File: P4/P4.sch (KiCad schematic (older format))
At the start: 113 parts, among them J1 Conn_01x10, J11 Conn_01x10, J12 Conn_01x10, J13 Conn_01x25, J14 Conn_01x25, J15 Conn_01x25, J16 Conn_01x25, J17 Conn_01x25, J18 Conn_01x25, J19 Conn_01x25, J2 Conn_01x10, J20 Conn_01x25, J26 Conn_01x01, J3 Conn_01x10, J4 Conn_01x10, J5 Conn_01x05, J6 Conn_01x10, J7 Conn_01x10, J8 Conn_01x03, J9 Conn_01x03, Q1 BC212L, Q2 BC212L, Q3 TIP42, Q4 TIP41, U1 LM723_DIP14, U10 LM13600, U11 LF353, U12 LM741, U13 LM13600, U2 LM741, U3 L7905, U4 LM1458, U5 LM1458, U6 LF353, U7 LM13600, U8 LF353, U9 LF353

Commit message: PS4 pcb layout
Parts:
- added H1, H10, H2, H3, H4, H5, H6, H7, H8, H9: MountingHole, MountingHole:MountingHole_3.2mm_M3_Pad, symbol Mechanical:MountingHole
- added HS1, HS2, HS3: Heatsink, Heatsink:Heatsink_Stonecold_HS-132_32x14mm_2xFixation1.5mm, symbol Mechanical:Heatsink
- C1, C13, C14, C2, C3, C4, C8, CA15, CA17, CA19, CA21, CB16, CB18, CB20, CB22: footprint (none) -> Capacitor_THT:C_Disc_D5.0mm_W2.5mm_P5.00mm
- C10, C11, C12, C7, C9: footprint (none) -> Capacitor_THT:CP_Radial_D6.3mm_P2.50mm
- C5, C6: footprint (none) -> Capacitor_THT:CP_Axial_L20.0mm_D13.0mm_P26.00mm_Horizontal
- D5, D6: footprint (none) -> Diode_THT:D_DO-15_P12.70mm_Horizontal
- J1, J11, J12, J2, J3, J4: footprint (none) -> Connector_PinHeader_2.54mm:PinHeader_1x10_P2.54mm_Vertical
- J13, J14, J15, J16, J17, J18, J19, J20: footprint (none) -> Connector_PinSocket_2.54mm:PinSocket_1x25_P2.54mm_Vertical
- J26: footprint (none) -> Connector_Wire:SolderWire-1.5sqmm_1x01_D1.7mm_OD3.9mm
- J5: footprint (none) -> Connector_PinHeader_2.54mm:PinHeader_1x05_P2.54mm_Vertical
- J6: renamed from J7; footprint (none) -> Connector_PinHeader_2.54mm:PinHeader_1x10_P2.54mm_Vertical
- J7: renamed from J6; footprint (none) -> Connector_PinHeader_2.54mm:PinHeader_1x10_P2.54mm_Vertical
- J8, J9: footprint (none) -> Connector_PinHeader_2.54mm:PinHeader_1x03_P2.54mm_Vertical
- Q1, Q2: footprint (none) -> Package_TO_SOT_THT:TO-92L_Wide
- R1, R10, R11, R12, R13, R14, R15, R16, R17, R18, R19, R2, R20, R21, R22, R23, R24, R25, R26, R27, R28, R29, R3, R4, R42, R43, R44, R5, R6, R7, R8, R9, RA30, RA33, RA36, RA39, RB31, RB34, RB37, RB40, RC32, RC35, RC38, RC41: footprint (none) -> Resistor_THT:R_Axial_DIN0207_L6.3mm_D2.5mm_P7.62mm_Horizontal
- RV1: footprint (none) -> Potentiometer_THT:Potentiometer_Bourns_3296Y_Vertical
- U10, U13, U7: footprint (none) -> Package_DIP:DIP-16_W7.62mm_Socket_LongPads
- U11, U12, U2, U4, U5, U6, U8, U9: footprint (none) -> Package_DIP:DIP-8_W7.62mm_Socket_LongPads
- U3: footprint (none) -> Package_TO_SOT_THT:TO-220-3_Vertical
- ZD1, ZD2: footprint (none) -> Diode_THT:D_DO-15_P10.16mm_Horizontal
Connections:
- net GNDA is gone; now on net GND: J6.10 (Pin_10), J6.9 (Pin_9), J7.5 (Pin_5), J7.6 (Pin_6)
- net at RV1.1: now also R14.1; no longer R13.2
- net at RV1.3: now also R13.2; no longer R14.1
- net 12_VCA_D renamed 14_VCA_D
- net 14_VCA_D: now also J2.4 (Pin_4); no longer J2.2 (Pin_2)
- net 14_VCA_R renamed 12_VCA_R
- net 12_VCA_R: now also J2.2 (Pin_2); no longer J2.4 (Pin_4)
- net U1_PIN10: no longer names the net of Q4.1 (B), U1.10 (Vout)
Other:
- moved on the sheet: J6, J7

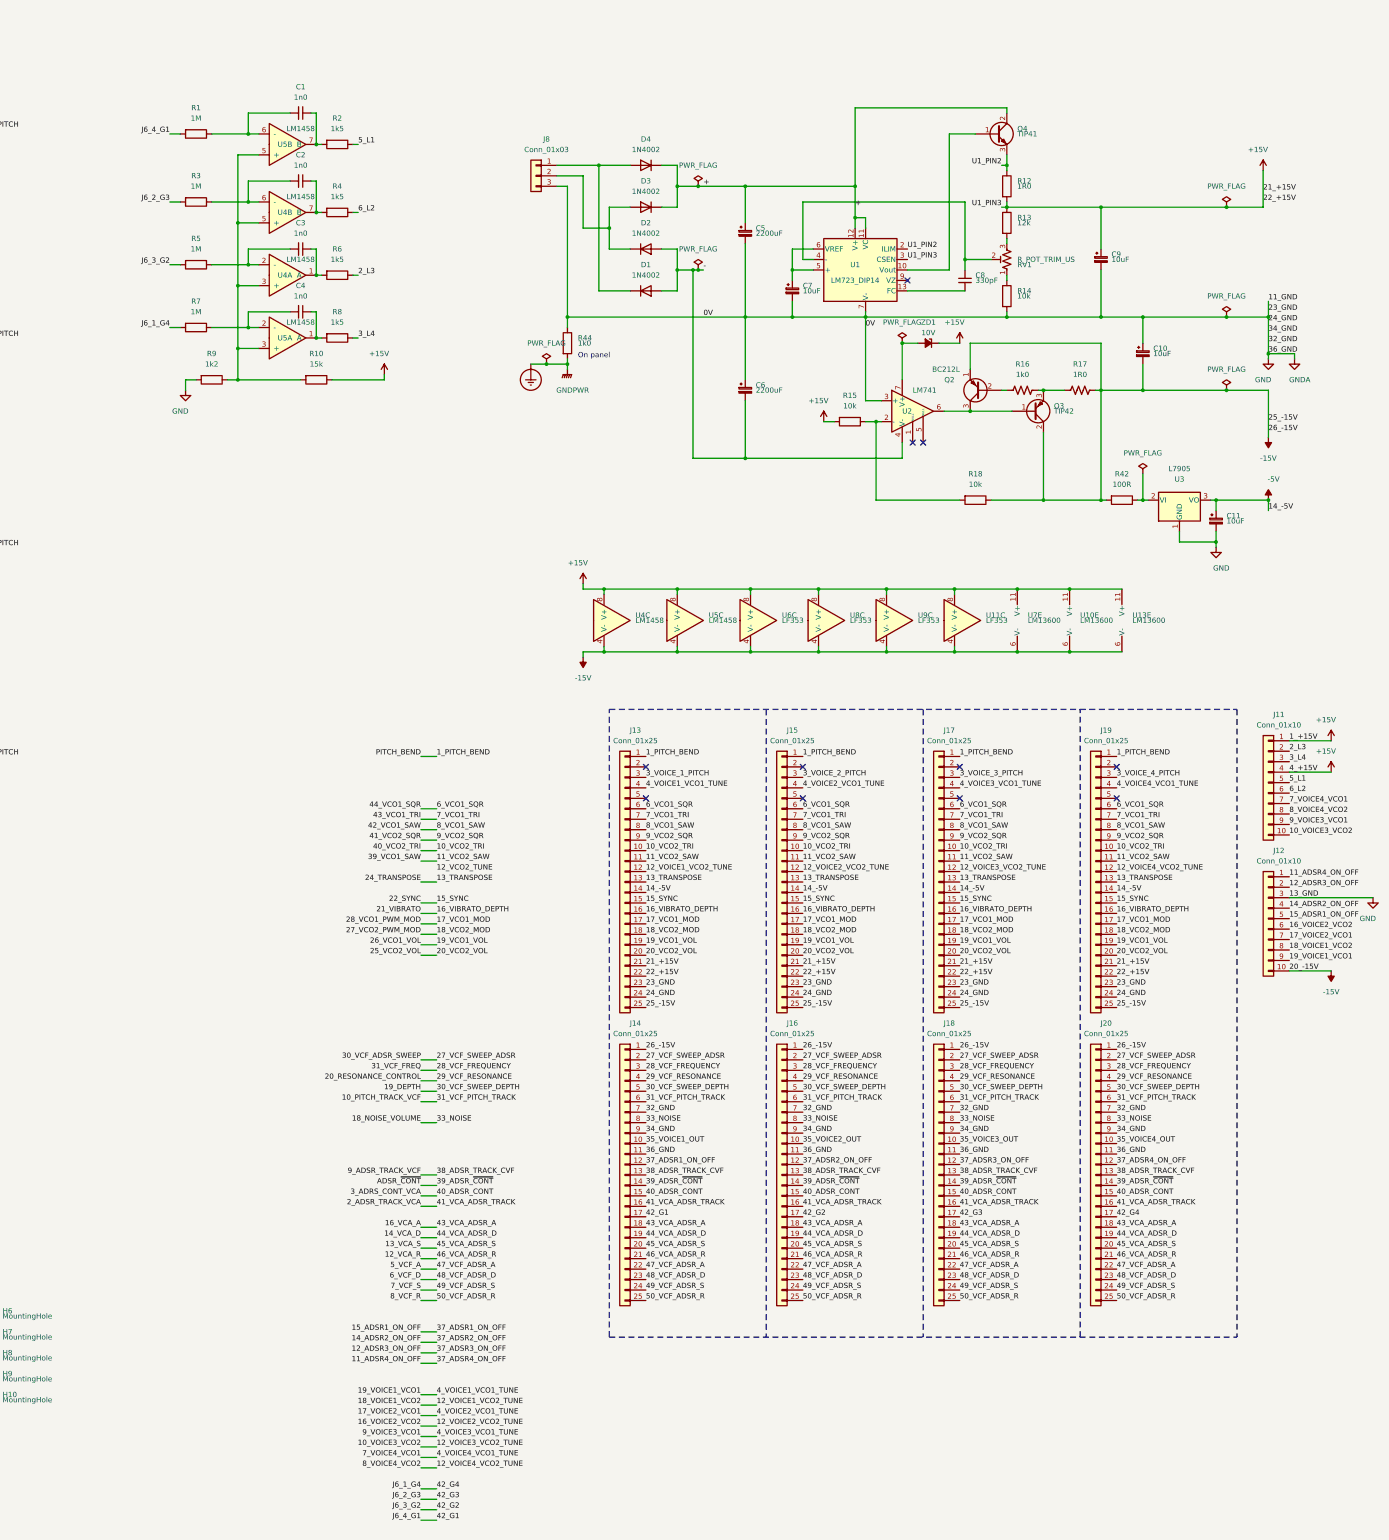
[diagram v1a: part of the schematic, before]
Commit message: Update PS4 board/schematic
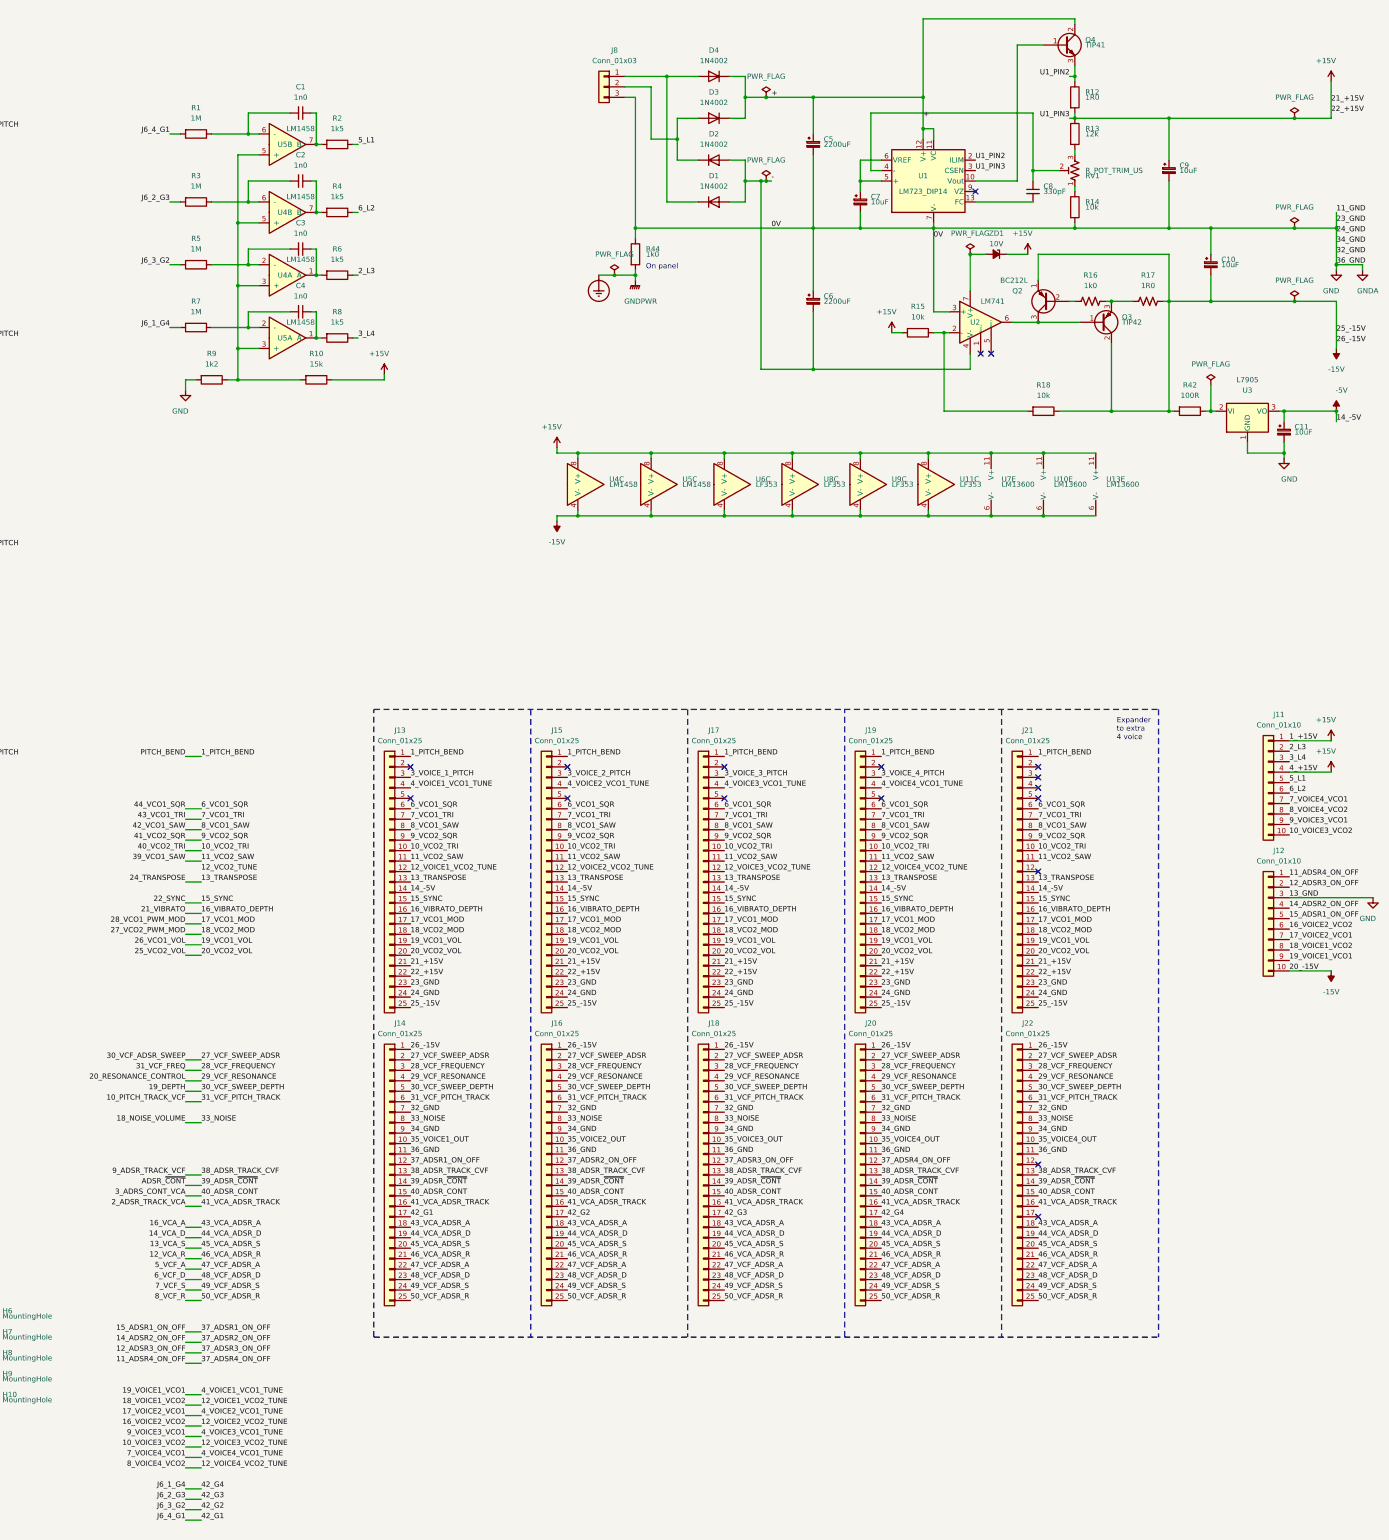
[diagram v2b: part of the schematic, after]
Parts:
- added J21, J22: Conn_01x25, Connector_PinSocket_2.54mm:PinSocket_1x25_P2.54mm_Vertical, symbol Connector_Generic:Conn_01x25
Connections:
- net +15V: now also J21.21 (Pin_21), J21.22 (Pin_22)
- net -15V: now also J21.25 (Pin_25), J22.1 (Pin_1)
- net -5V: now also J21.14 (Pin_14)
- net 10_PITCH_TRACK_VCF: now also J22.6 (Pin_6)
- net 10_VCO2_TRI: now also J21.10 (Pin_10)
- net 11_VCO2_SAW: now also J21.11 (Pin_11)
- net 12_VCA_R: now also J22.21 (Pin_21)
- net 13_TRANSPOSE: now also J21.13 (Pin_13)
- net 13_VCA_S: now also J22.20 (Pin_20)
- net 14_VCA_D: now also J22.19 (Pin_19)
- net 15_SYNC: now also J21.15 (Pin_15)
- net 16_VCA_A: now also J22.18 (Pin_18)
- net 16_VIBRATO_DEPTH: now also J21.16 (Pin_16)
- net 17_VCO1_MOD: now also J21.17 (Pin_17)
- net 18_NOISE_VOLUME: now also J22.8 (Pin_8)
- net 18_VCO2_MOD: now also J21.18 (Pin_18)
- net 19_DEPTH: now also J22.5 (Pin_5)
- net 19_VCO1_VOL: now also J21.19 (Pin_19)
- net 1_PITCH_BEND: now also J21.1 (Pin_1)
- net 20_RESONANCE_CONTROL: now also J22.4 (Pin_4)
- net 20_VCO2_VOL: now also J21.20 (Pin_20)
- net 27_VCF_SWEEP_ADSR: now also J22.2 (Pin_2)
- net 28_VCF_FREQUENCY: now also J22.3 (Pin_3)
- net 2_ADSR_TRACK_VCA: now also J22.16 (Pin_16)
- net 35_VOICE1_OUT: now also J22.10 (Pin_10)
- net 38_ADSR_TRACK_CVF: now also J22.13 (Pin_13)
- net 39_ADSR_~CONT: now also J22.14 (Pin_14)
- net 3_ADRS_CONT_VCA: now also J22.15 (Pin_15)
- net 41_VCO2_SQR: now also J21.9 (Pin_9)
- net 42_VCO1_SAW: now also J21.8 (Pin_8)
- net 43_VCO1_TRI: now also J21.7 (Pin_7)
- net 44_VCO1_SQR: now also J21.6 (Pin_6)
- net 47_VCF_ADSR_A: now also J22.22 (Pin_22)
- net 48_VCF_ADSR_D: now also J22.23 (Pin_23)
- net 49_VCF_ADSR_S: now also J22.24 (Pin_24)
- net 50_VCF_ADSR_R: now also J22.25 (Pin_25)
- net GND: now also J21.23 (Pin_23), J21.24 (Pin_24), J22.11 (Pin_11), J22.7 (Pin_7), J22.9 (Pin_9)
- no-connect marks 36 -> 43
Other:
- note added: "Expander \nto extra \n4 voice"
- moved on the sheet: C10, C11, C5, C6, C7, C8, C9, D1, D2, D3, D4, J13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

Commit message: P4 layout in progress
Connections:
- net 3_VOICE_1_PITCH: now also U11.2 (-), U11.6 (-), U11.7 (B); no longer U6.2 (-), U6.6 (-), U6.7 (B)
- net 3_VOICE_2_PITCH: now also U9.2 (-), U9.6 (-), U9.7 (B); no longer U8.2 (-), U8.6 (-), U8.7 (B)
- net 3_VOICE_3_PITCH: now also U8.2 (-), U8.6 (-), U8.7 (B); no longer U9.2 (-), U9.6 (-), U9.7 (B)
- net 3_VOICE_4_PITCH: now also U6.2 (-), U6.6 (-), U6.7 (B); no longer U11.2 (-), U11.6 (-), U11.7 (B)
- net 42_G2: now also R3.2; no longer R5.2
- net 42_G3: now also R5.2; no longer R3.2
- net P1: now also U11.3 (+); no longer U6.3 (+)
- net P2: now also U9.3 (+); no longer U8.3 (+)
- net P3: now also U8.3 (+); no longer U9.3 (+)
- net P4: now also U6.3 (+); no longer U11.3 (+)
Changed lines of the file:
@@
 $EndDescr
 $Comp
-L Regulator_Linear:LM723_DIP14 U1
-U 1 1 5EEB4956
-P 18450 2200
-F 0 "U1" H 18350 2250 50  0000 C CNN
-F 1 "LM723_DIP14" H 18350 2100 50  0000 C CNN
-F 2 "Package_DIP:DIP-14_W7.62mm" H 18475 1850 50  0001 L CNN
-F 3 "http://www.ti.com/lit/ds/symlink/lm723.pdf" H 18350 2100 50  0001 C CNN
-	1    18450 2200
-	1    0    0    -1
-$EndComp
-$Comp
 L Amplifier_Operational:LM741 U2
 U 1 1 5EEB4E2D
@@
 	6650 1600 6700 1600
 Connection ~ 6700 1600
-Text Label 6000 1500 2    50   ~ 0
+Text Label 6000 7500 2    50   ~ 0
 P1
 Wire Wire Line
@@
 Wire Wire Line
 	4250 1550 4250 1450
-Text Label 8400 1050 0    50   ~ 0
+Text Label 8400 7050 0    50   ~ 0
 VOICE1_PORTAMENTO
 Wire Wire Line
@@
 	6650 3600 6700 3600
 Connection ~ 6700 3600
-Text Label 6000 3500 2    50   ~ 0
+Text Label 6000 5500 2    50   ~ 0
 P2
 Wire Wire Line
@@
 Wire Wire Line
 	7200 2750 7200 2800
-Text Label 8400 3050 0    50   ~ 0
+Text Label 8400 5050 0    50   ~ 0
 VOICE2_PORTAMENTO
 Wire Wire Line
@@
 	6650 5600 6700 5600
 Connection ~ 6700 5600
-Text Label 6000 5500 2    50   ~ 0
+Text Label 6000 3500 2    50   ~ 0
 P3
 Wire Wire Line
@@
 Wire Wire Line
 	7200 4750 7200 4800
-Text Label 8400 5050 0    50   ~ 0
+Text Label 8400 3050 0    50   ~ 0
 VOICE3_PORTAMENTO
 Wire Wire Line
@@
 	6650 7600 6700 7600
 Connection ~ 6700 7600
-Text Label 6000 7500 2    50   ~ 0
+Text Label 6000 1500 2    50   ~ 0
 P4
 Wire Wire Line
@@
 Wire Wire Line
 	7200 6750 7200 6800
-Text Label 8400 7050 0    50   ~ 0
+Text Label 8400 1050 0    50   ~ 0
 VOICE4_PORTAMENTO
 Wire Wire Line
@@
 Text Label 13450 7900 0    50   ~ 0
 3_VOICE_1_PITCH
-Text Label 9100 1700 0    50   ~ 0
+Text Label 9100 7700 0    50   ~ 0
 3_VOICE_1_PITCH
 Text Label 13450 8000 0    50   ~ 0
@@
 Wire Wire Line
 	11300 13500 11450 13500
-Text Label 9100 3700 0    50   ~ 0
-3_VOICE_2_PITCH
 Text Label 9100 5700 0    50   ~ 0
+3_VOICE_2_PITCH
+Text Label 9100 3700 0    50   ~ 0
 3_VOICE_3_PITCH
-Text Label 9100 7700 0    50   ~ 0
+Text Label 9100 1700 0    50   ~ 0
 3_VOICE_4_PITCH
 Text Label 11300 13800 2    50   ~ 0
@@
 Text Label 11150 3600 2    50   ~ 0
 J6_1_G4
-Text Label 11150 2400 2    50   ~ 0
-J6_2_G3
 Text Label 11150 3000 2    50   ~ 0
+J6_2_G3
+Text Label 11150 2400 2    50   ~ 0
 J6_3_G2
 Text Label 11150 1750 2    50   ~ 0
@@
 NoConn ~ 19450 12100
 NoConn ~ 19450 11600
+$Comp
+L Regulator_Linear:LM723_DIP14 U1
+U 1 1 625ABC7E
+P 18450 2200
+F 0 "U1" H 18400 2200 50  0000 C CNN
+F 1 "LM723_DIP14" H 18350 2050 50  0000 C CNN
+F 2 "Package_DIP:DIP-14_W7.62mm" H 18475 1850 50  0001 L CNN
+F 3 "http://www.ti.com/lit/ds/symlink/lm723.pdf" H 18350 2100 50  0001 C CNN
+	1    18450 2200
+	1    0    0    -1
+$EndComp
 $EndSCHEMATC
